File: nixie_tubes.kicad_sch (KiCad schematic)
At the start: 6 parts

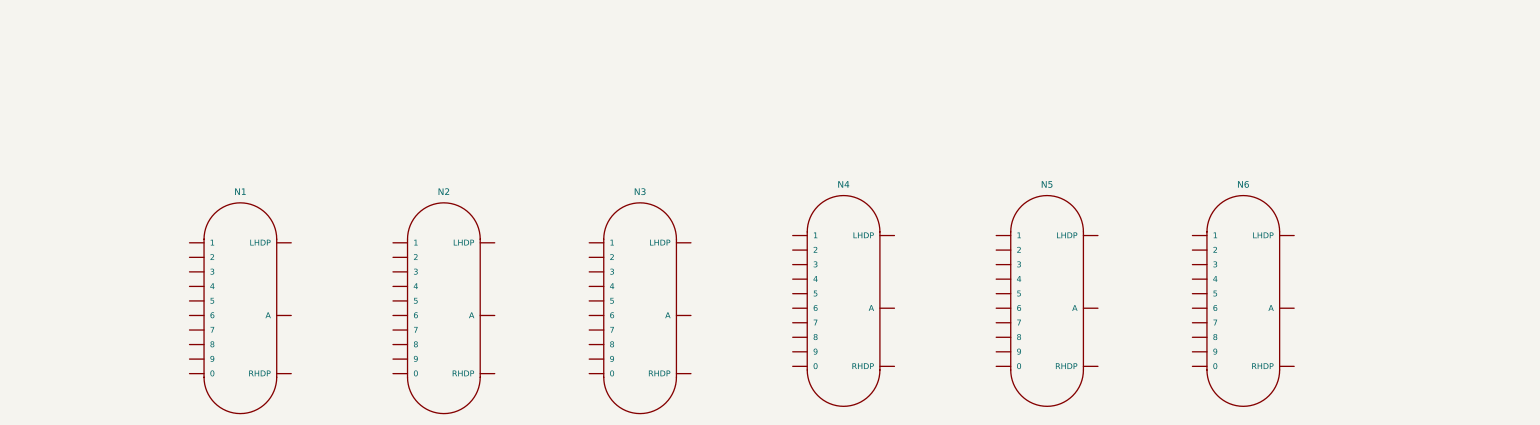
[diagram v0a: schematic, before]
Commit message: Add current limiting resistors and net labels to nixie tubes
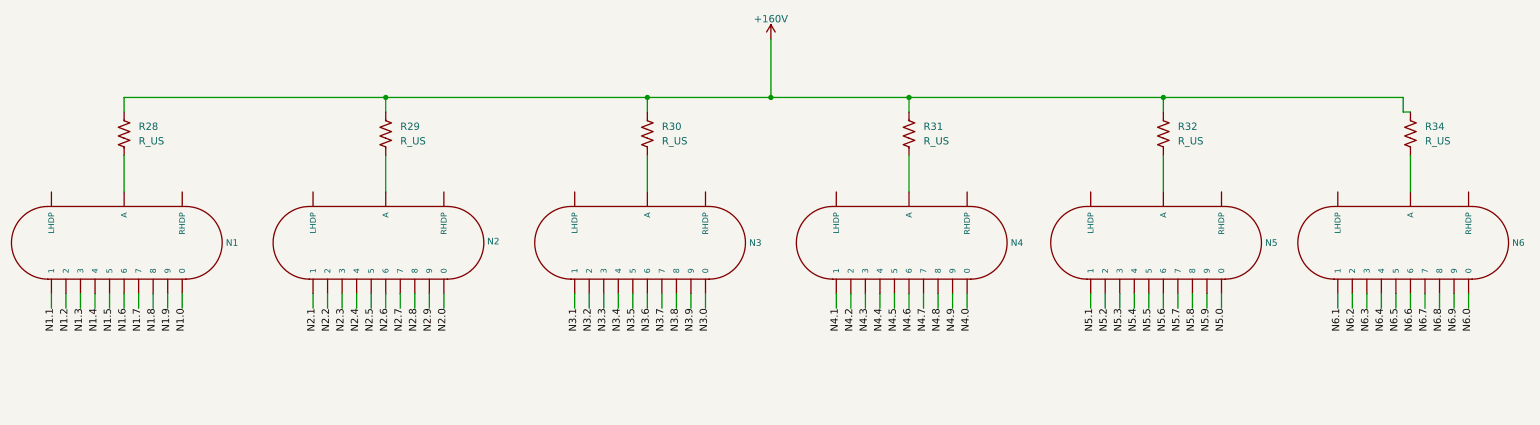
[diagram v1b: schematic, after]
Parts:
- added R28, R29, R30, R31, R32, R34: R_US, symbol Device:R_US
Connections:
- net N3.0: now reaches N3.0
- net N3.1: now reaches N3.1
- net N3.2: now reaches N3.2
- net N3.3: now reaches N3.3
- net N3.4: now reaches N3.4
- net N3.5: now reaches N3.5
- net N3.6: now reaches N3.6
- net N3.7: now reaches N3.7
- net N3.8: now reaches N3.8
- net N3.9: now reaches N3.9
- net at N3.A: now also R30.2
- net N5.0: now reaches N5.0
- net N5.1: now reaches N5.1
- net N5.2: now reaches N5.2
- net N5.3: now reaches N5.3
- net N5.4: now reaches N5.4
- net N5.5: now reaches N5.5
- net N5.6: now reaches N5.6
- net N5.7: now reaches N5.7
- net N5.8: now reaches N5.8
- net N5.9: now reaches N5.9
- net at N5.A: now also R32.2
- net N6.0: now reaches N6.0
- net N6.1: now reaches N6.1
- net N6.2: now reaches N6.2
- net N6.3: now reaches N6.3
- net N6.4: now reaches N6.4
- net N6.5: now reaches N6.5
- net N6.6: now reaches N6.6
- net N6.7: now reaches N6.7
- net N6.8: now reaches N6.8
- net N6.9: now reaches N6.9
- net at N6.A: now also R34.2
- net N2.0: now reaches N2.0
- net N2.1: now reaches N2.1
- net N2.2: now reaches N2.2
- net N2.3: now reaches N2.3
- net N2.4: now reaches N2.4
- net N2.5: now reaches N2.5
- net N2.6: now reaches N2.6
- net N2.7: now reaches N2.7
- net N2.8: now reaches N2.8
- net N2.9: now reaches N2.9
- net at N2.A: now also R29.2
- net N4.0: now reaches N4.0
- net N4.1: now reaches N4.1
- net N4.2: now reaches N4.2
- net N4.3: now reaches N4.3
- net N4.4: now reaches N4.4
- net N4.5: now reaches N4.5
- net N4.6: now reaches N4.6
- net N4.7: now reaches N4.7
- net N4.8: now reaches N4.8
- net N4.9: now reaches N4.9
- net at N4.A: now also R31.2
- net N1.0: now reaches N1.0
- net N1.1: now reaches N1.1
- net N1.2: now reaches N1.2
- net N1.3: now reaches N1.3
- net N1.4: now reaches N1.4
- net N1.5: now reaches N1.5
- net N1.6: now reaches N1.6
- net N1.7: now reaches N1.7
- net N1.8: now reaches N1.8
- net N1.9: now reaches N1.9
- net at N1.A: now also R28.2
- new net +160V: R28.1, R29.1, R30.1, R31.1, R32.1, R34.1
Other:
- moved on the sheet: N1
